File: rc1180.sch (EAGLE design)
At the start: 19 parts, among them J1 47642-0001, U1 CH340C, U2 AMS1117, X1 SMA-142-0701-801/806

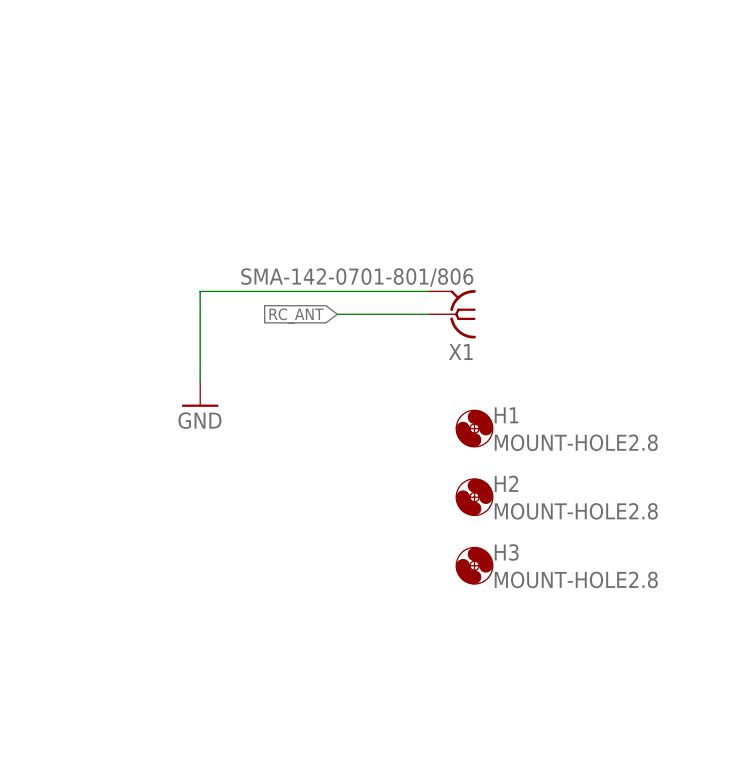
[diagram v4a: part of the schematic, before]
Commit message: Added matching circuit for antenna
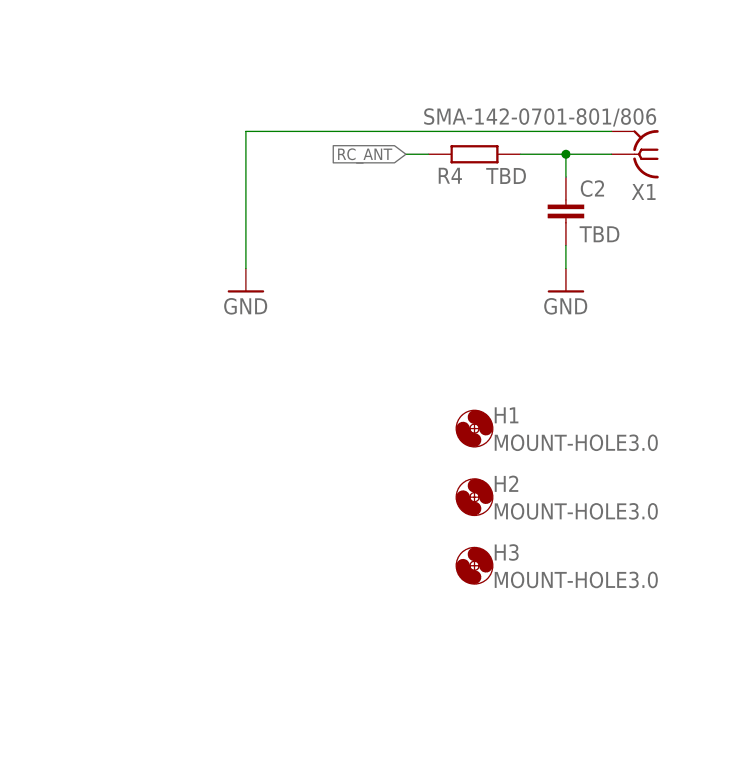
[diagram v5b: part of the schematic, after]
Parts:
- added C2: TBD, rcl:C-EUC0805
- added R4: TBD, rcl:R-EU_R0805
- H1, H2, H3: value MOUNT-HOLE2.8 -> MOUNT-HOLE3.0; device holes:MOUNT-HOLE2.8 -> holes:MOUNT-HOLE3.0
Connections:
- new net N$3: C2.1, R4.2, X1.1
- net GND: now also C2.2
- net RC_ANT: now also R4.1; no longer X1.1
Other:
- moved on the sheet: X1
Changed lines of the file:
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@@
 <part name="X1" library="con-coax" library_urn="urn:adsk.eagle:library:133" deviceset="SMA-" device="142-0701-801/806" package3d_urn="urn:adsk.eagle:package:6214/1"/>
 <part name="GND13" library="supply1" library_urn="urn:adsk.eagle:library:371" deviceset="GND" device=""/>
-<part name="H1" library="holes" library_urn="urn:adsk.eagle:library:237" deviceset="MOUNT-HOLE" device="2.8" package3d_urn="urn:adsk.eagle:package:14271/1"/>
-<part name="H2" library="holes" library_urn="urn:adsk.eagle:library:237" deviceset="MOUNT-HOLE" device="2.8" package3d_urn="urn:adsk.eagle:package:14271/1"/>
-<part name="H3" library="holes" library_urn="urn:adsk.eagle:library:237" deviceset="MOUNT-HOLE" device="2.8" package3d_urn="urn:adsk.eagle:package:14271/1"/>
+<part name="H1" library="holes" library_urn="urn:adsk.eagle:library:237" deviceset="MOUNT-HOLE" device="3.0" package3d_urn="urn:adsk.eagle:package:14277/1" value="MOUNT-HOLE3.0"/>
+<part name="H2" library="holes" library_urn="urn:adsk.eagle:library:237" deviceset="MOUNT-HOLE" device="3.0" package3d_urn="urn:adsk.eagle:package:14277/1" value="MOUNT-HOLE3.0"/>
+<part name="H3" library="holes" library_urn="urn:adsk.eagle:library:237" deviceset="MOUNT-HOLE" device="3.0" package3d_urn="urn:adsk.eagle:package:14277/1" value="MOUNT-HOLE3.0"/>
+<part name="R4" library="rcl" library_urn="urn:adsk.eagle:library:334" deviceset="R-EU_" device="R0805" package3d_urn="urn:adsk.eagle:package:23553/2" value="TBD"/>
+<part name="C2" library="rcl" library_urn="urn:adsk.eagle:library:334" deviceset="C-EU" device="C0805" package3d_urn="urn:adsk.eagle:package:23617/2" value="TBD"/>
+<part name="GND6" library="supply1" library_urn="urn:adsk.eagle:library:371" deviceset="GND" device=""/>
 </parts>
 <sheets>
@@
 <attribute name="SHEET" x="230.505" y="5.08" size="2.54" layer="94"/>
 </instance>
-<instance part="X1" gate="G1" x="215.9" y="139.7" smashed="yes" rot="R180">
-<attribute name="VALUE" x="218.44" y="144.78" size="1.778" layer="96" rot="R180"/>
-<attribute name="NAME" x="218.44" y="136.398" size="1.778" layer="95" rot="R180"/>
-</instance>
-<instance part="GND13" gate="1" x="187.96" y="129.54" smashed="yes">
-<attribute name="VALUE" x="185.42" y="127" size="1.778" layer="96"/>
+<instance part="X1" gate="G1" x="236.22" y="157.48" smashed="yes" rot="R180">
+<attribute name="VALUE" x="238.76" y="162.56" size="1.778" layer="96" rot="R180"/>
+<attribute name="NAME" x="238.76" y="154.178" size="1.778" layer="95" rot="R180"/>
+</instance>
+<instance part="GND13" gate="1" x="193.04" y="142.24" smashed="yes">
+<attribute name="VALUE" x="190.5" y="139.7" size="1.778" layer="96"/>
 </instance>
 <instance part="H1" gate="G$1" x="218.44" y="127" smashed="yes">
@@
 <attribute name="NAME" x="220.472" y="112.3442" size="1.778" layer="95"/>
 <attribute name="VALUE" x="220.472" y="109.2962" size="1.778" layer="96"/>
+</instance>
+<instance part="R4" gate="G$1" x="218.44" y="157.48" smashed="yes">
+<attribute name="NAME" x="217.17" y="155.9814" size="1.778" layer="95" rot="R180"/>
+<attribute name="VALUE" x="224.282" y="155.956" size="1.778" layer="96" rot="R180"/>
+</instance>
+<instance part="C2" gate="G$1" x="228.6" y="152.4" smashed="yes">
+<attribute name="NAME" x="230.124" y="152.781" size="1.778" layer="95"/>
+<attribute name="VALUE" x="230.124" y="147.701" size="1.778" layer="96"/>
+</instance>
+<instance part="GND6" gate="1" x="228.6" y="142.24" smashed="yes">
+<attribute name="VALUE" x="226.06" y="139.7" size="1.778" layer="96"/>
 </instance>
 </instances>
@@
 </segment>
 <segment>
+<pinref part="GND6" gate="1" pin="GND"/>
+<pinref part="C2" gate="G$1" pin="2"/>
+<wire x1="228.6" y1="144.78" x2="228.6" y2="147.32" width="0.1524" layer="91"/>
+</segment>
+<segment>
 <pinref part="X1" gate="G1" pin="2"/>
-<wire x1="213.36" y1="142.24" x2="187.96" y2="142.24" width="0.1524" layer="91"/>
 <pinref part="GND13" gate="1" pin="GND"/>
-<wire x1="187.96" y1="142.24" x2="187.96" y2="132.08" width="0.1524" layer="91"/>
+<wire x1="233.68" y1="160.02" x2="193.04" y2="160.02" width="0.1524" layer="91"/>
+<wire x1="193.04" y1="160.02" x2="193.04" y2="144.78" width="0.1524" layer="91"/>
 </segment>
 </net>
@@
 </segment>
 <segment>
-<pinref part="X1" gate="G1" pin="1"/>
-<wire x1="213.36" y1="139.7" x2="203.2" y2="139.7" width="0.1524" layer="91"/>
-<label x="203.2" y="139.7" size="1.27" layer="95" rot="R180" xref="yes"/>
+<pinref part="R4" gate="G$1" pin="1"/>
+<wire x1="213.36" y1="157.48" x2="210.82" y2="157.48" width="0.1524" layer="91"/>
+<label x="210.82" y="157.48" size="1.27" layer="95" rot="R180" xref="yes"/>
 </segment>
 </net>
@@
 </segment>
 </net>
+<net name="N$3" class="0">
+<segment>
+<pinref part="R4" gate="G$1" pin="2"/>
+<pinref part="X1" gate="G1" pin="1"/>
+<wire x1="223.52" y1="157.48" x2="228.6" y2="157.48" width="0.1524" layer="91"/>
+<pinref part="C2" gate="G$1" pin="1"/>
+<wire x1="228.6" y1="157.48" x2="233.68" y2="157.48" width="0.1524" layer="91"/>
+<wire x1="228.6" y1="154.94" x2="228.6" y2="157.48" width="0.1524" layer="91"/>
+<junction x="228.6" y="157.48"/>
+</segment>
+</net>

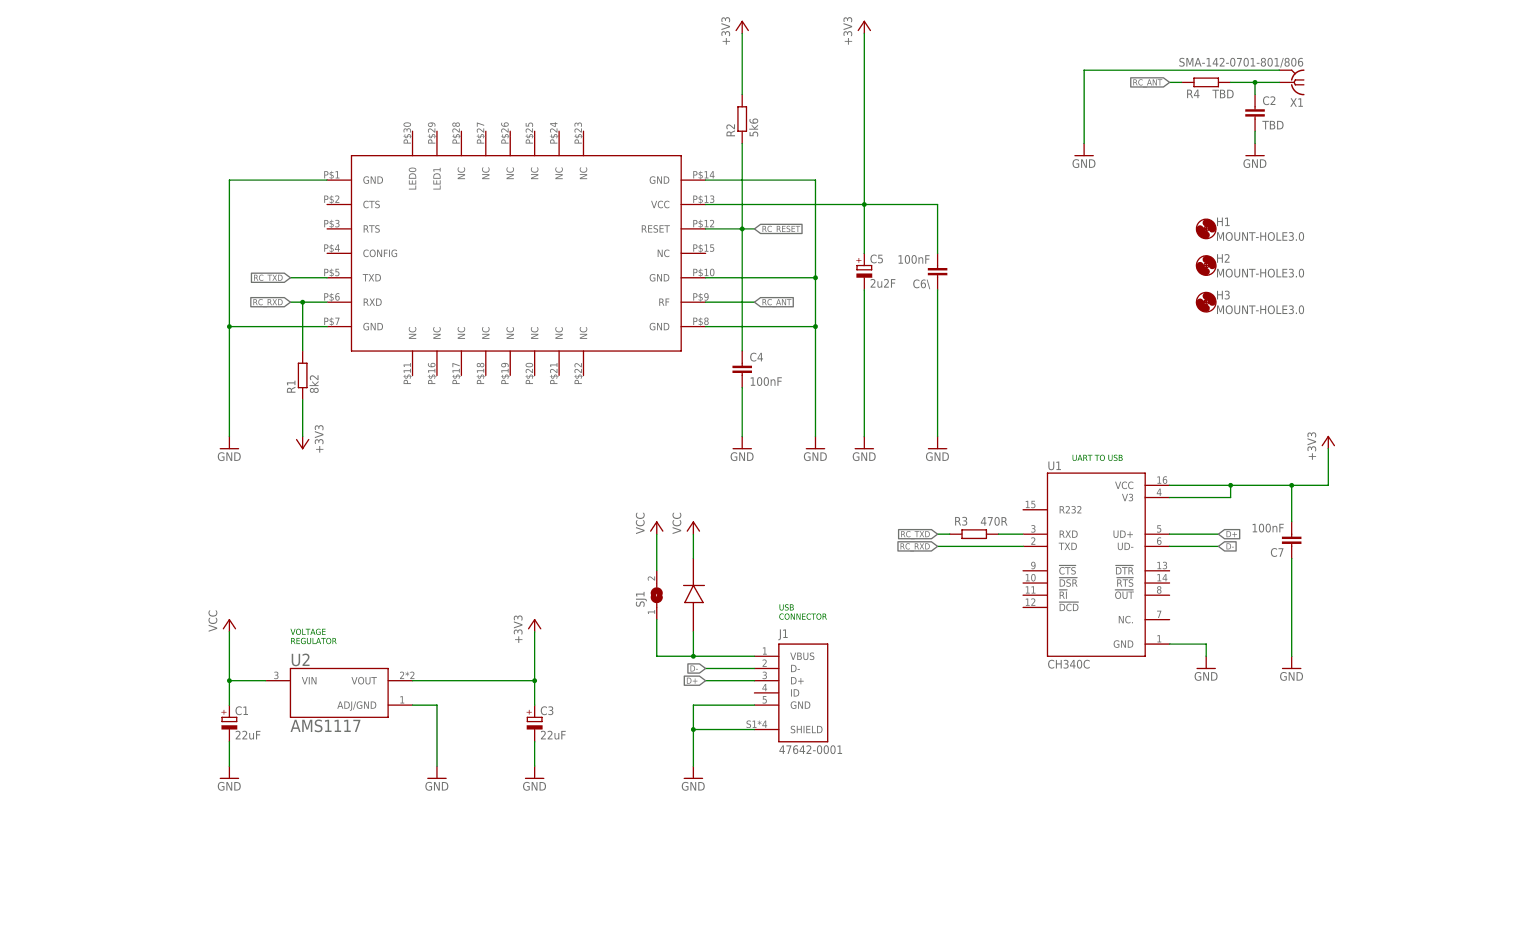
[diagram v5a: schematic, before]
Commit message: Updated 100nF caps to be the same
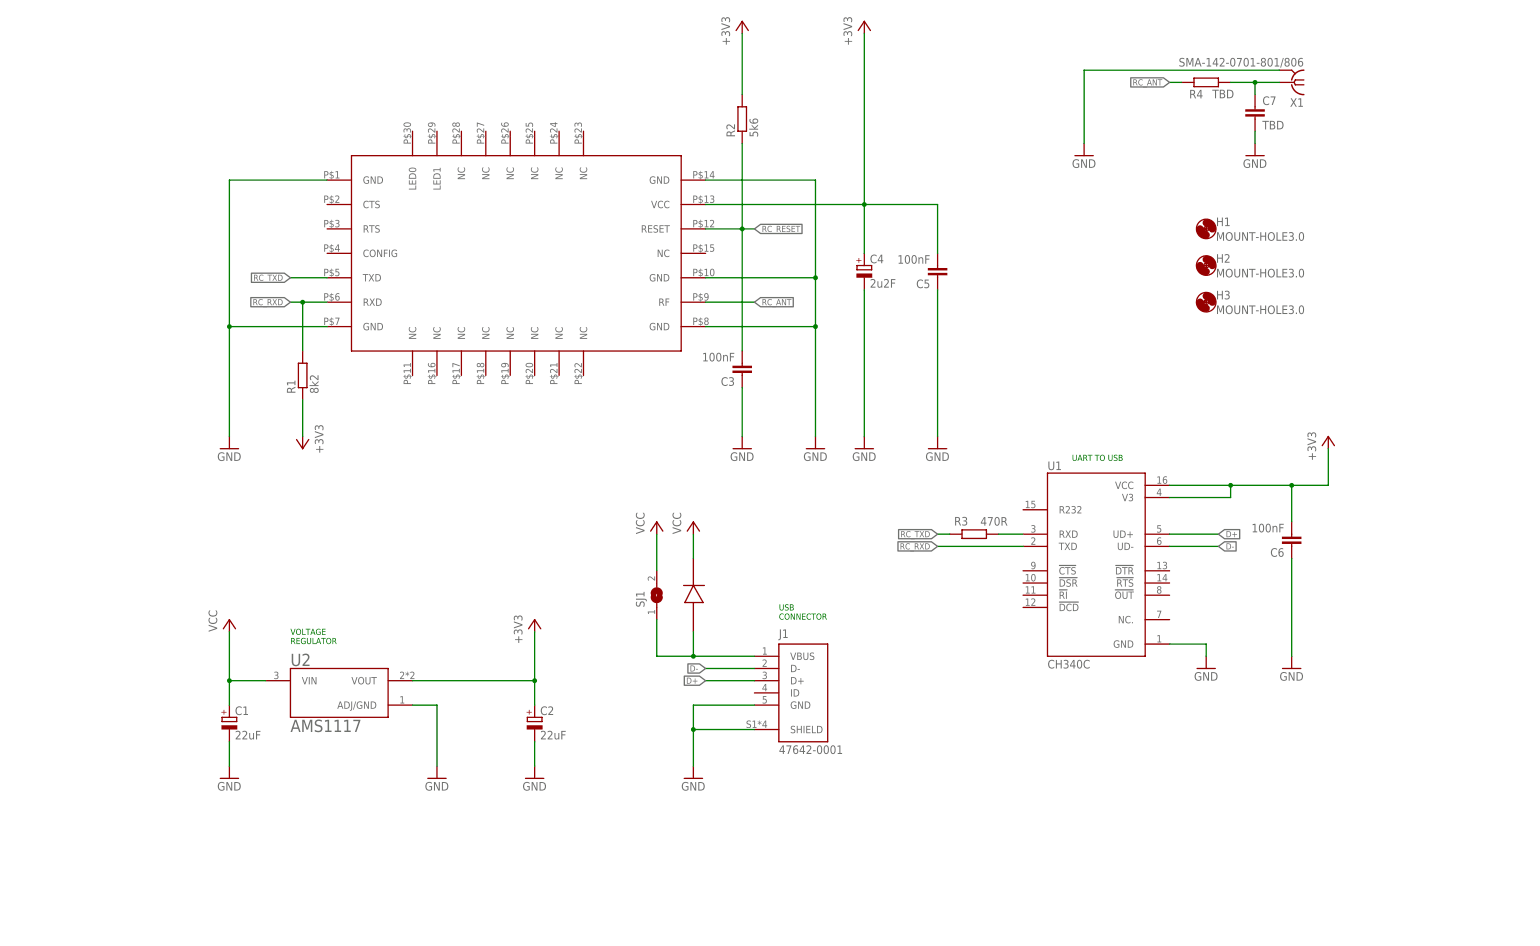
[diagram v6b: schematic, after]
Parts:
- removed C6\: 100nF, rcl:C-EUC0805K
- added C6: 100nF, rcl:C-EUC0805K
- C2: value TBD -> 22uF; device rcl:C-EUC0805 -> rcl:CPOL-EUC/6032-28R; TME_PN (none) -> 293D226X9010C2TE3
- C3: value 22uF -> 100nF; device rcl:CPOL-EUC/6032-28R -> rcl:C-EUC0805K; TME_PN 293D226X9010C2TE3 -> (none)
- C4: value 100nF -> 2u2F; device rcl:C-EUC0805 -> rcl:CPOL-EUA/3216-18W; TME_PN (none) -> T491A225K020AT
- C5: value 2u2F -> 100nF; device rcl:CPOL-EUA/3216-18W -> rcl:C-EUC0805K; TME_PN T491A225K020AT -> (none)
- C7: value 100nF -> TBD; device rcl:C-EUC0805K -> rcl:C-EUC0603
- R4: device rcl:R-EU_R0805 -> rcl:R-EU_R0603
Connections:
- net +3V3: now also C2.+, C4.+, C5.2, C6.2; no longer C3.+, C5.+, C6\.2, C7.2
- net GND: now also C2.-, C3.1, C4.-, C5.1, C6.1, C7.2; no longer C2.2, C3.-, C4.2, C5.-, C6\.1, C7.1
- net N$3: now also C7.1; no longer C2.1
- net RC_RESET: now also C3.2; no longer C4.1
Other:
- moved on the sheet: C7

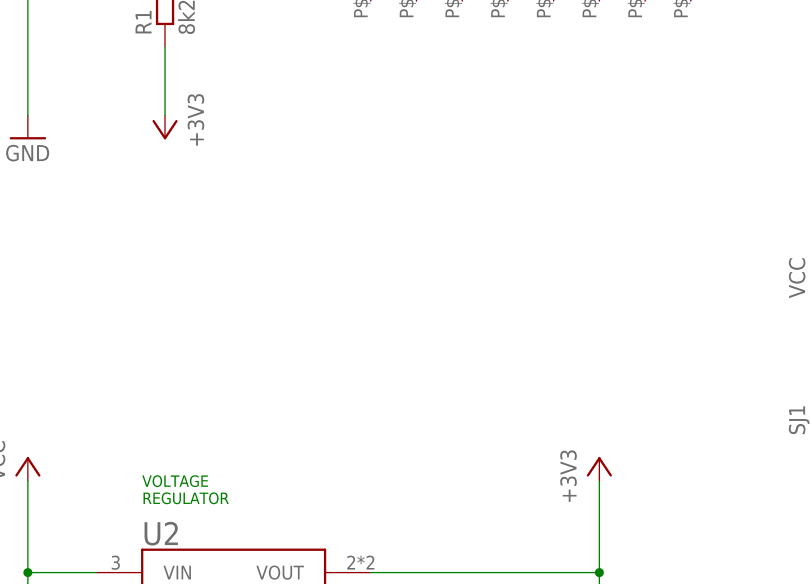
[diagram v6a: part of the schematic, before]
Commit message: Added vias and testpoints
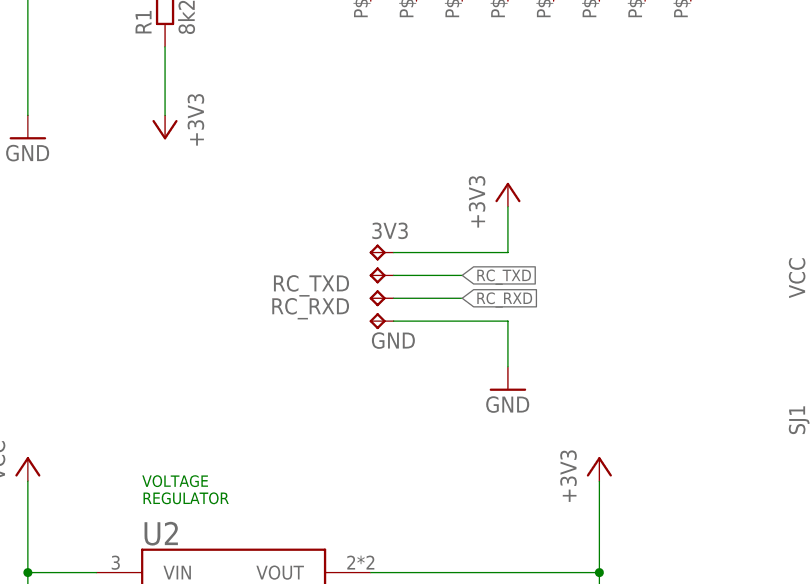
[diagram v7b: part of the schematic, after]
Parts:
- added 3V3, GND, RC_RXD, RC_TXD: TPB1,27, testpad:TPB1,27
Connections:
- net +3V3: now also 3V3.TP
- net GND: now also GND.TP
- net RC_RXD: now also RC_RXD.TP
- net RC_TXD: now also RC_TXD.TP
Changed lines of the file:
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@@
 <part name="C7" library="rcl" library_urn="urn:adsk.eagle:library:334" deviceset="C-EU" device="C0603" package3d_urn="urn:adsk.eagle:package:23616/2" value="TBD"/>
 <part name="C3" library="rcl" library_urn="urn:adsk.eagle:library:334" deviceset="C-EU" device="C0805K" package3d_urn="urn:adsk.eagle:package:23681/2" value="100nF"/>
+<part name="GND14" library="supply1" library_urn="urn:adsk.eagle:library:371" deviceset="GND" device=""/>
+<part name="+3V6" library="supply1" library_urn="urn:adsk.eagle:library:371" deviceset="+3V3" device=""/>
+<part name="GND" library="testpad" library_urn="urn:adsk.eagle:library:385" deviceset="TP" device="B1,27" package3d_urn="urn:adsk.eagle:package:27944/2" value="TPB1,27"/>
+<part name="RC_RXD" library="testpad" library_urn="urn:adsk.eagle:library:385" deviceset="TP" device="B1,27" package3d_urn="urn:adsk.eagle:package:27944/2" value="TPB1,27"/>
+<part name="RC_TXD" library="testpad" library_urn="urn:adsk.eagle:library:385" deviceset="TP" device="B1,27" package3d_urn="urn:adsk.eagle:package:27944/2" value="TPB1,27"/>
+<part name="3V3" library="testpad" library_urn="urn:adsk.eagle:library:385" deviceset="TP" device="B1,27" package3d_urn="urn:adsk.eagle:package:27944/2" value="TPB1,27"/>
 </parts>
 <sheets>
@@
 <attribute name="VALUE" x="120.396" y="101.219" size="1.778" layer="96" rot="R180"/>
 </instance>
+<instance part="GND14" gate="1" x="68.58" y="53.34" smashed="yes">
+<attribute name="VALUE" x="66.04" y="50.8" size="1.778" layer="96"/>
+</instance>
+<instance part="+3V6" gate="G$1" x="68.58" y="76.2" smashed="yes">
+<attribute name="VALUE" x="66.04" y="71.12" size="1.778" layer="96" rot="R90"/>
+</instance>
+<instance part="GND" gate="G$1" x="53.34" y="60.96" smashed="yes" rot="R90">
+<attribute name="NAME" x="53.34" y="57.912" size="1.778" layer="95"/>
+<attribute name="TP_SIGNAL_NAME" x="54.61" y="62.23" size="1.778" layer="97" rot="R90"/>
+</instance>
+<instance part="RC_RXD" gate="G$1" x="53.34" y="63.5" smashed="yes" rot="R90">
+<attribute name="NAME" x="51.054" y="63.5" size="1.778" layer="95" rot="R180"/>
+<attribute name="TP_SIGNAL_NAME" x="54.61" y="64.77" size="1.778" layer="97" rot="R90"/>
+</instance>
+<instance part="RC_TXD" gate="G$1" x="53.34" y="66.04" smashed="yes" rot="R90">
+<attribute name="NAME" x="51.054" y="66.04" size="1.778" layer="95" rot="R180"/>
+<attribute name="TP_SIGNAL_NAME" x="54.61" y="67.31" size="1.778" layer="97" rot="R90"/>
+</instance>
+<instance part="3V3" gate="G$1" x="53.34" y="68.58" smashed="yes" rot="R90">
+<attribute name="NAME" x="53.34" y="70.104" size="1.778" layer="95"/>
+<attribute name="TP_SIGNAL_NAME" x="54.61" y="69.85" size="1.778" layer="97" rot="R90"/>
+</instance>
 </instances>
 <busses>
@@
 <wire x1="233.68" y1="160.02" x2="193.04" y2="160.02" width="0.1524" layer="91"/>
 <wire x1="193.04" y1="160.02" x2="193.04" y2="144.78" width="0.1524" layer="91"/>
+</segment>
+<segment>
+<pinref part="GND14" gate="1" pin="GND"/>
+<wire x1="55.88" y1="60.96" x2="68.58" y2="60.96" width="0.1524" layer="91"/>
+<wire x1="68.58" y1="60.96" x2="68.58" y2="55.88" width="0.1524" layer="91"/>
+<pinref part="GND" gate="G$1" pin="TP"/>
 </segment>
 </net>
@@
 <junction x="78.74" y="33.02"/>
 </segment>
+<segment>
+<wire x1="55.88" y1="68.58" x2="68.58" y2="68.58" width="0.1524" layer="91"/>
+<wire x1="68.58" y1="68.58" x2="68.58" y2="73.66" width="0.1524" layer="91"/>
+<pinref part="+3V6" gate="G$1" pin="+3V3"/>
+<pinref part="3V3" gate="G$1" pin="TP"/>
+</segment>
 </net>
 <net name="RC_TXD" class="0">
@@
 <wire x1="165.1" y1="63.5" x2="162.56" y2="63.5" width="0.1524" layer="91"/>
 <label x="162.56" y="63.5" size="1.27" layer="95" rot="R180" xref="yes"/>
+</segment>
+<segment>
+<wire x1="55.88" y1="66.04" x2="63.5" y2="66.04" width="0.1524" layer="91"/>
+<label x="63.5" y="66.04" size="1.27" layer="95" xref="yes"/>
+<pinref part="RC_TXD" gate="G$1" pin="TP"/>
 </segment>
 </net>
@@
 <label x="162.56" y="60.96" size="1.27" layer="95" rot="R180" xref="yes"/>
 </segment>
+<segment>
+<wire x1="55.88" y1="63.5" x2="63.5" y2="63.5" width="0.1524" layer="91"/>
+<label x="63.5" y="63.5" size="1.27" layer="95" xref="yes"/>
+<pinref part="RC_RXD" gate="G$1" pin="TP"/>
+</segment>
 </net>
